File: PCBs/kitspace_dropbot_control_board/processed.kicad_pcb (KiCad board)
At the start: 4 copper layers, 115 x 92 mm, 141 parts, among them P1 CONN_01X01, P10 CONN_01X01, P11 TFM-105-02-X-DH, P2 CONN_01X01, P3 CONN_01X03, P4 CONN_01X02, P5 CONN_01X01, P6 USB_B, P7 CONN_01X04, P8 CONN_01X03, P9 USB_A, Q1 STP33N65M2, Q5 IRF740BPBF, Q6 IRF740BPBF, SW1 PROG, U1 Teensy_3.2, U10 IS25LP064A-JBLE, U11 MCP6022, U12 DPST (2 Form A), 350V, U2 MAX1771, U3 CAT5171, U4 HV7802, U5 DPST (2 Form A), 350V, U6 NCP5304, U7 DPST (2 Form A), 350V, U8 DPST (2 Form A), 350V, U9 74AHC1G32

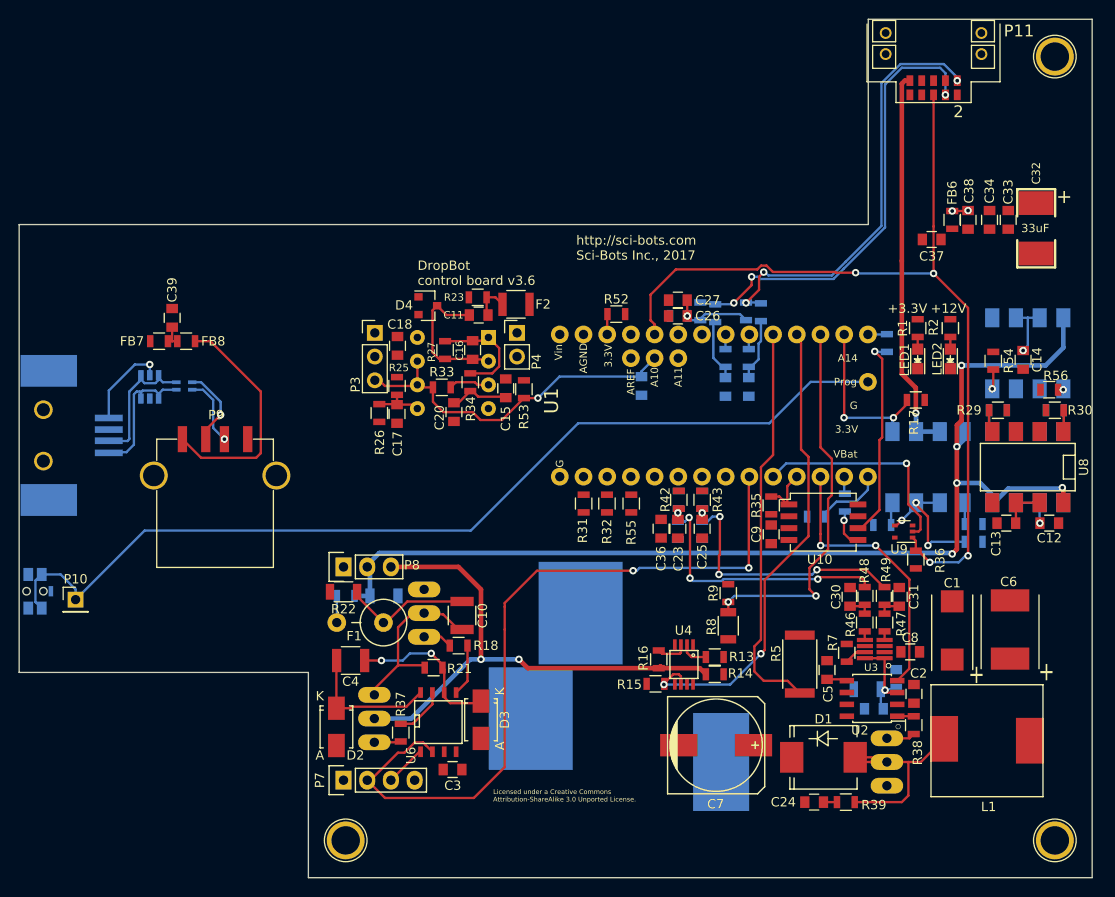
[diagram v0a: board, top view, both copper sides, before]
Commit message: recheck all circuits and clean up fill zone by rerouting the nets using freerouting and manually
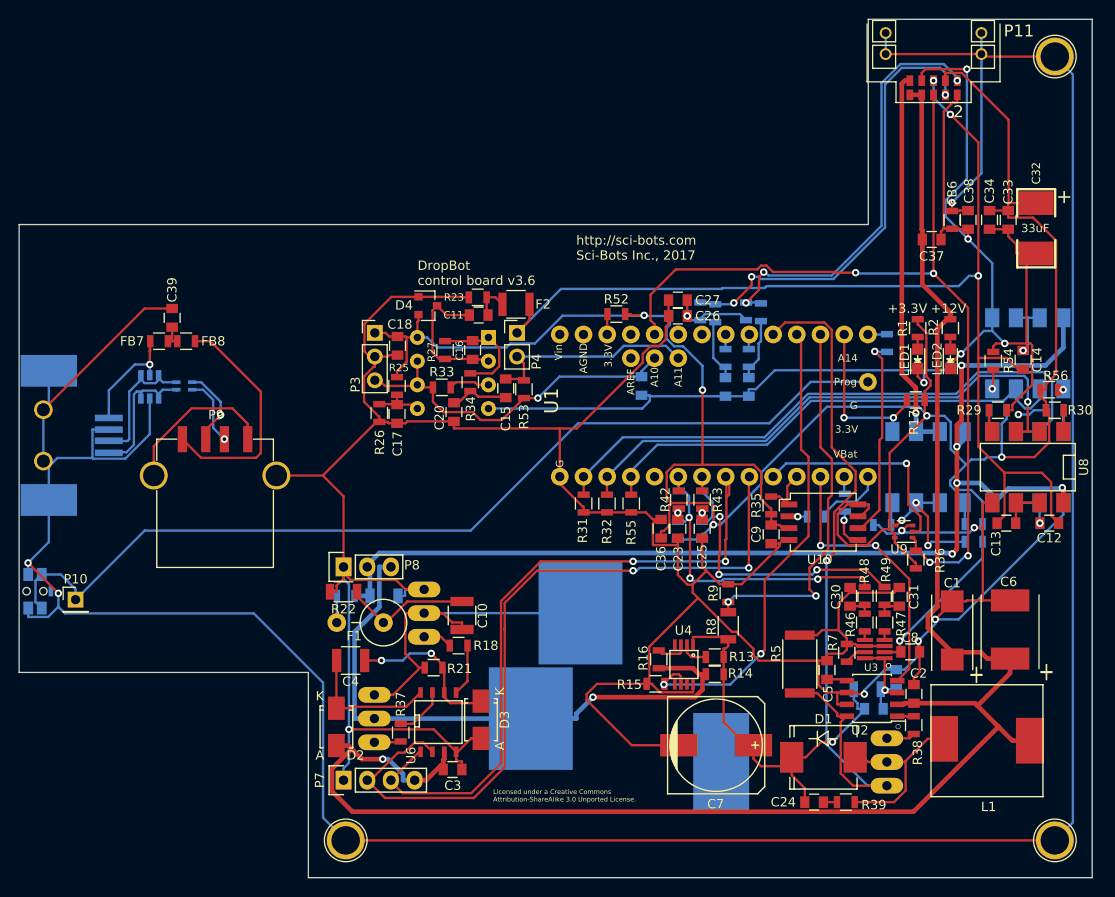
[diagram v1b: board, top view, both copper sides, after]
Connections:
- C1 pad 1: (no net) -> +12V
- C1 pad 2: (no net) -> GND
- C12 pad 1: (no net) -> Net-(C12-Pad1)
- C12 pad 2: (no net) -> CUR_SENSE
- C13 pad 2: (no net) -> CUR_SENSE
- C14 pad 1: (no net) -> Net-(C14-Pad1)
- C14 pad 2: (no net) -> CUR_SENSE
- C15 pad 2: (no net) -> A11
- C17 pad 2: (no net) -> GND
- C18 pad 1: (no net) -> +3V3
- C18 pad 2: (no net) -> GND
- C19 pad 2: (no net) -> Net-(C19-Pad2)
- C2 pad 1: (no net) -> GND
- C2 pad 2: (no net) -> +12V
- C20 pad 1: (no net) -> GND
- C21 pad 1: (no net) -> GND
- C22 pad 1: (no net) -> GND
- C23 pad 2: (no net) -> GND
- C24 pad 1: (no net) -> Net-(C19-Pad2)
- C25 pad 1: (no net) -> GND
- C26 pad 1: (no net) -> GND
- C27 pad 1: (no net) -> GND
- C28 pad 2: (no net) -> GND
- C29 pad 1: (no net) -> GND
- C3 pad 1: (no net) -> GND
- C3 pad 2: (no net) -> +12V
- C30 pad 2: (no net) -> GND
- C31 pad 1: (no net) -> GND
- C32 pad 1: (no net) -> +3V3
- C32 pad 2: (no net) -> GND
- C33 pad 1: (no net) -> GND
- C33 pad 2: (no net) -> +3V3
- C34 pad 1: (no net) -> GND
- C34 pad 2: (no net) -> +3V3
- C35 pad 1: (no net) -> GND
- C36 pad 1: (no net) -> GND
- C36 pad 2: (no net) -> +3V3
- C37 pad 1: (no net) -> GND
- C37 pad 2: (no net) -> +12V
- C38 pad 2: (no net) -> GND
- C39 pad 1: (no net) -> CHASIS_GND
- C5 pad 2: (no net) -> GND
- C6 pad 1: (no net) -> +12V
- C6 pad 2: (no net) -> GND
- C7 pad 1: (no net) -> Net-(C19-Pad2)
- C7 pad 2: (no net) -> GND
- C8 pad 1: (no net) -> GND
- C8 pad 2: (no net) -> +3V3
- C9 pad 1: (no net) -> +3V3
- C9 pad 2: (no net) -> GND
- D1 pad 1: (no net) -> Net-(C19-Pad2)
- D2 pad 2: (no net) -> +12V
- D3 pad 2: (no net) -> GND
- D4 pad 1: (no net) -> GND
- D4 pad 2: (no net) -> +3V3
- D5 pad 2: (no net) -> CHASIS_GND
- F2 pad 2: (no net) -> CUR_SENSE
- FB1 pad 2: (no net) -> +3V3
- FB3 pad 2: (no net) -> Net-(FB3-Pad2)
- FB6 pad 1: (no net) -> GND
- FB7 pad 1: (no net) -> Net-(D5-Pad5)
- L1 pad 2: (no net) -> +12V
- LED1 pad 1: (no net) -> GND
- LED2 pad 1: (no net) -> GND
- P1 pad 1: (no net) -> CHASIS_GND
- P11 pad 1: (no net) -> SDA
- P11 pad 10: (no net) -> +12V
- P11 pad 2: (no net) -> GND
- P11 pad 3: (no net) -> +3V3
- P11 pad 4: (no net) -> SCL
- P11 pad 5: (no net) -> CUR_SENSE
- P11 pad 7: (no net) -> GND
- P11 pad 8: (no net) -> +12V
- P11 pad G1: (no net) -> CHASIS_GND
- P11 pad G2: (no net) -> CHASIS_GND
- P11 pad G3: (no net) -> CHASIS_GND
- P11 pad G4: (no net) -> CHASIS_GND
- P2 pad 1: (no net) -> CHASIS_GND
- P3 pad 1: (no net) -> +3V3
- P3 pad 2: (no net) -> GND
- P4 pad 1: (no net) -> CUR_SENSE
- P4 pad 2: (no net) -> A11
- P5 pad 1: (no net) -> CHASIS_GND
- P6 pad 4: (no net) -> CHASIS_GND
- P6 pad 5: (no net) -> CHASIS_GND
- P7 pad 1: (no net) -> GND
- P7 pad 4: (no net) -> +12V
- P8 pad 1: (no net) -> GND
- P9 pad 3: (no net) -> /USB pass-through/D+
- P9 pad 4: (no net) -> GND
- P9 pad 5: (no net) -> GND
- Q1 pad 3: (no net) -> A3/MAX1771_CS
- Q6 pad 2: (no net) -> Net-(C10-Pad1)
- Q6 pad 3: (no net) -> GND
- R1 pad 1: (no net) -> +3V3
- R10 pad 1: (no net) -> +3V3
- R11 pad 1: (no net) -> GND
- R12 pad 1: (no net) -> +3V3
- R13 pad 1: (no net) -> Net-(C19-Pad2)
- R14 pad 2: (no net) -> Net-(C19-Pad2)
- R15 pad 1: (no net) -> GND
- R17 pad 1: (no net) -> +3V3
- R19 pad 2: (no net) -> +3V3
- R2 pad 1: (no net) -> +12V
- R20 pad 2: (no net) -> +3V3
- R22 pad 2: (no net) -> GND
- R23 pad 2: (no net) -> GND
- R24 pad 1: (no net) -> GND
- R25 pad 1: (no net) -> +3V3
- R26 pad 2: (no net) -> GND
- R28 pad 1: (no net) -> +3V3
- R29 pad 1: (no net) -> GND
- R30 pad 1: (no net) -> +3V3
- R31 pad 1: (no net) -> D0
- R31 pad 2: (no net) -> GND
- R32 pad 1: (no net) -> D1
- R32 pad 2: (no net) -> GND
- R35 pad 2: (no net) -> +3V3
- R36 pad 2: (no net) -> +3V3
- R4 pad 2: (no net) -> SCL
- R40 pad 2: (no net) -> D4/SSDA
- R41 pad 2: (no net) -> D5/SSCL
- R42 pad 1: (no net) -> Net-(R42-Pad1)
- R43 pad 1: (no net) -> Net-(R43-Pad1)
- R5 pad 2: (no net) -> GND
- R52 pad 1: (no net) -> +3V3
- R53 pad 1: (no net) -> A11
- R54 pad 1: (no net) -> GND
- R55 pad 1: (no net) -> D2
- R55 pad 2: (no net) -> GND
- R56 pad 1: (no net) -> +3V3
- R6 pad 1: (no net) -> Net-(C19-Pad2)
- R7 pad 2: (no net) -> GND
- R8 pad 2: (no net) -> Net-(C19-Pad2)
- R9 pad 1: (no net) -> GND
- SW1 pad 2: (no net) -> CHASIS_GND
- U1 pad 0: (no net) -> D0
- U1 pad 1: (no net) -> D1
- U1 pad 2: (no net) -> D2
- U1 pad 20: (no net) -> Net-(U1-Pad20)
- U1 pad 21: (no net) -> Net-(U1-Pad21)
- U1 pad 23: (no net) -> Net-(U1-Pad23)
- U1 pad 25: (no net) -> Net-(U1-Pad25)
- U1 pad 26: (no net) -> Net-(U1-Pad26)
- U1 pad 27: (no net) -> GND
- U1 pad 3: (no net) -> Net-(U1-Pad3)
- U1 pad 33: (no net) -> A11
- U1 pad 35: (no net) -> Net-(U1-Pad35)
- U1 pad 4: (no net) -> Net-(R42-Pad1)
- U1 pad 5: (no net) -> Net-(R43-Pad1)
- U1 pad 6: (no net) -> D6/DRIVER_LO
- U10 pad 1: (no net) -> D9/CS
- U10 pad 2: (no net) -> Net-(FB3-Pad2)
- U10 pad 3: (no net) -> +3V3
- U10 pad 4: (no net) -> GND
- U10 pad 7: (no net) -> +3V3
- U10 pad 8: (no net) -> +3V3
- U11 pad 4: (no net) -> GND
- U11 pad 8: (no net) -> +3V3
- U12 pad 2: (no net) -> D2
- U12 pad 3: (no net) -> D2
- U12 pad 4: (no net) -> Net-(R54-Pad2)
- U12 pad 5: (no net) -> GND
- U2 pad 2: (no net) -> +12V
- U2 pad 6: (no net) -> GND
- U2 pad 7: (no net) -> GND
- U2 pad 8: (no net) -> A3/MAX1771_CS
- U3 pad 2: (no net) -> +3V3
- U3 pad 3: (no net) -> GND
- U3 pad 6: (no net) -> GND
- U4 pad 1: (no net) -> Net-(C19-Pad2)
- U4 pad 8: (no net) -> GND
- U6 pad 3: (no net) -> +12V
- U6 pad 4: (no net) -> GND
- U7 pad 2: (no net) -> D0
- U7 pad 3: (no net) -> D0
- U7 pad 5: (no net) -> GND
- U8 pad 2: (no net) -> D1
- U8 pad 3: (no net) -> D1
- U8 pad 5: (no net) -> GND
- U9 pad 3: (no net) -> GND
- U9 pad 5: (no net) -> +3V3
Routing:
- net GND: track 0.00 -> 567.9 mm, vias 0 -> 12
- net CHASIS_GND: track 1.72 -> 327.0 mm, vias 2 -> 3
- net +3V3: track 0.00 -> 281.1 mm, vias 0 -> 6
- net +12V: track 0.00 -> 191.9 mm, vias 0 -> 1
- net CUR_SENSE: track 0.00 -> 122.5 mm, vias 0 -> 3
- net D6/DRIVER_LO: track 4.44 -> 72.5 mm, vias 0 -> 2
- net D0: track 0.00 -> 66.4 mm
- net D1: track 0.00 -> 60.8 mm, vias 0 -> 1
- net D2: track 0.00 -> 53.0 mm
- net Net-(C19-Pad2): track 0.00 -> 42.8 mm, vias 0 -> 1
- net A3/MAX1771_CS: track 42.8 -> 80.4 mm, vias 0 -> 1
- net A11: track 0.00 -> 23.2 mm
- net Net-(C10-Pad1): track 19.4 -> 37.1 mm
- net HV: track 57.5 -> 64.4 mm, vias 2 -> 1
- net Net-(D1-Pad2): track 24.0 -> 19.9 mm
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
